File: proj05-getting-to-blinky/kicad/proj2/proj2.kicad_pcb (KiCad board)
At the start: 2 copper layers, 48.3 x 48.3 mm, 7 parts, among them U1 NTE955MC

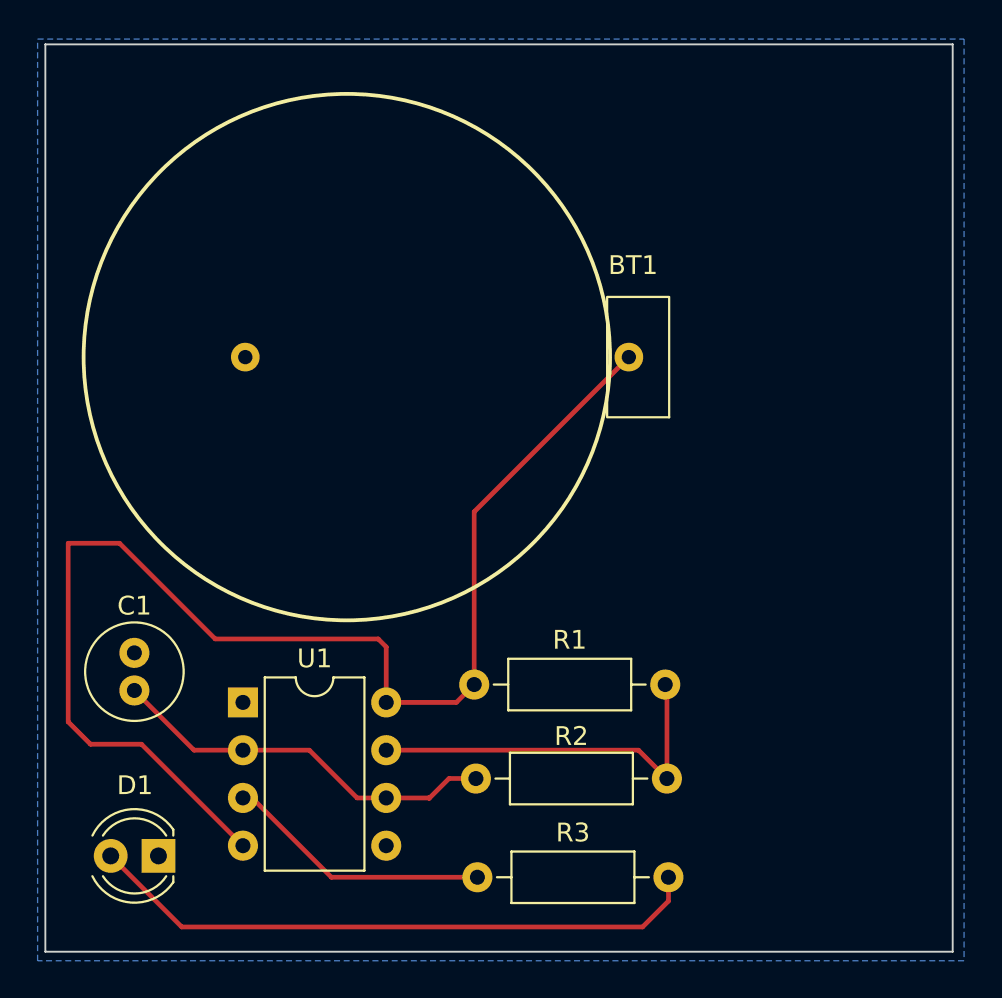
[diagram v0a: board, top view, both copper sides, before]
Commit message: add artwork to proj5
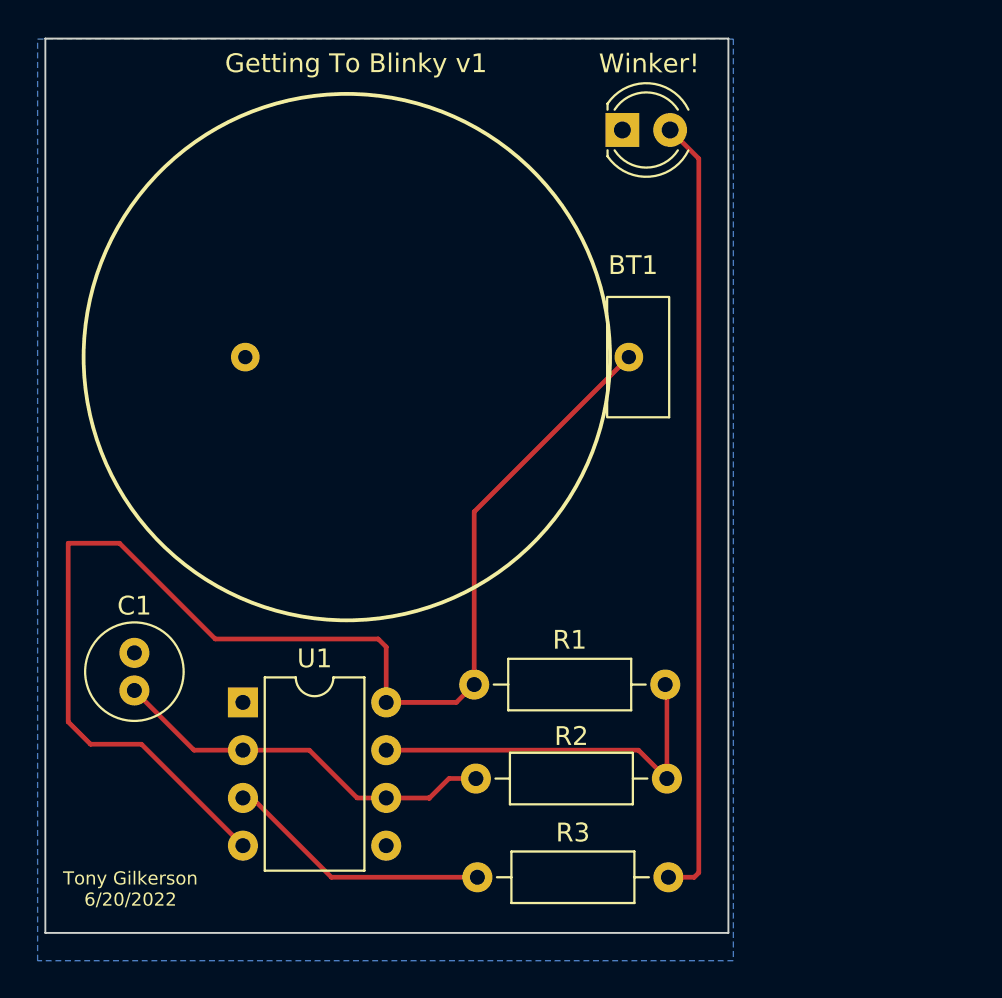
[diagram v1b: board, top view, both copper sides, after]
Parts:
- moved Winker! 45.8 mm to (141.1, 81.3), turned to 0 degrees
- renumbered D1 to Winker!
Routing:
- net Net-(D1-Pad2): track 33.1 -> 41.8 mm
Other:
- board size 48.3 x 48.3 mm -> 36.3 x 47.6 mm
- board text added: "Getting To Blinky v1"
- board text added: "Tony Gilkerson 6/20/2022"
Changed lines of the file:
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@@
   )
   (setup
+    (stackup
+      (layer "F.SilkS" (type "Top Silk Screen"))
+      (layer "F.Paste" (type "Top Solder Paste"))
+      (layer "F.Mask" (type "Top Solder Mask") (thickness 0.01))
+      (layer "F.Cu" (type "copper") (thickness 0.035))
+      (layer "dielectric 1" (type "core") (thickness 1.51) (material "FR4") (epsilon_r 4.5) (loss_tangent 0.02))
+      (layer "B.Cu" (type "copper") (thickness 0.035))
+      (layer "B.Mask" (type "Bottom Solder Mask") (thickness 0.01))
+      (layer "B.Paste" (type "Bottom Solder Paste"))
+      (layer "B.SilkS" (type "Bottom Silk Screen"))
+      (copper_finish "None")
+      (dielectric_constraints no)
+    )
     (pad_to_mask_clearance 0)
     (pcbplotparams
@@
   )
   (footprint "LED_THT:LED_D4.0mm" (layer "F.Cu")
-    (at 116.41 119.9 180)
+    (at 141.085 81.29)
     (descr "LED, diameter 4.0mm, 2 pins, http://www.kingbright.com/attachments/file/psearch/000/00/00/L-43GD(Ver.12B).pdf")
     (tags "LED diameter 4.0mm 2 pins")
@@
     (property "Sheetname" "")
     (attr through_hole)
-    (fp_text reference "D1" (at 1.25 3.75) (layer "F.SilkS")
-      (effects (font (size 1 1) (thickness 0.15)))
-    )
-    (fp_text value "LED" (at 1.27 -3.75) (layer "F.Fab")
+    (fp_text reference "Winker!" (at 1.425 -3.53) (layer "F.SilkS")
+      (effects (font (size 1 1) (thickness 0.15)))
+    )
+    (fp_text value "LED" (at 1.235 3.73) (layer "F.Fab")
       (effects (font (size 1 1) (thickness 0.15)))
     )
@@
     (fp_arc (start -0.73 -1.32665) (mid 3.67 0.000306) (end -0.730339 1.32614) (layer "F.Fab") (width 0.1))
     (fp_circle (center 1.27 0) (end 3.27 0) (layer "F.Fab") (width 0.1) (fill none))
-    (pad "1" thru_hole rect (at 0 0 180) (size 1.8 1.8) (drill 0.9) (layers *.Cu *.Mask)
+    (pad "1" thru_hole rect (at 0 0) (size 1.8 1.8) (drill 0.9) (layers *.Cu *.Mask)
       (net 2 "GND") (pinfunction "K") (pintype "passive"))
-    (pad "2" thru_hole circle (at 2.54 0 180) (size 1.8 1.8) (drill 0.9) (layers *.Cu *.Mask)
+    (pad "2" thru_hole circle (at 2.54 0) (size 1.8 1.8) (drill 0.9) (layers *.Cu *.Mask)
       (net 4 "Net-(D1-Pad2)") (pinfunction "A") (pintype "passive"))
     (model "${KICAD6_3DMODEL_DIR}/LED_THT.3dshapes/LED_D4.0mm.wrl"
@@
       (effects (font (size 1 1) (thickness 0.15)))
     )
-    (fp_text value "NTE955MC" (at 3.81 9.95) (layer "F.Fab")
-      (effects (font (size 1 1) (thickness 0.15)))
-    )
-    (fp_text user "${REFERENCE}" (at 3.81 3.81) (layer "F.Fab")
+    (fp_text value "NTE955MC" (at 3.786 10.244) (layer "F.Fab")
+      (effects (font (size 1 1) (thickness 0.15)))
+    )
+    (fp_text user "${REFERENCE}" (at 3.856 4.434) (layer "F.Fab")
       (effects (font (size 1 1) (thickness 0.15)))
     )
@@
     )
   )
-  (gr_rect (start 110.394 76.736) (end 158.654 124.996) (layer "Edge.Cuts") (width 0.1) (fill none))
+  (gr_line (start 121.15 81.44) (end 120.93 80.81) (layer "B.SilkS") (width 0.15))
+  (gr_line (start 115.91 82.37) (end 115.58 82.81) (layer "B.SilkS") (width 0.15))
+  (gr_circle (center 118.782918 83.97) (end 124.332918 80.87) (layer "B.SilkS") (width 0.15) (fill none))
+  (gr_line (start 121.65 81.44) (end 121.88 80.87) (layer "B.SilkS") (width 0.15))
+  (gr_arc (start 122.022432 85.648649) (mid 118.837206 88.08984) (end 115.542432 85.798649) (layer "B.SilkS") (width 0.2))
+  (gr_line (start 117.14 82.44) (end 117.54 82.89) (layer "B.SilkS") (width 0.15))
+  (gr_line (start 116.84 82.58) (end 117.03 83.08) (layer "B.SilkS") (width 0.15))
+  (gr_line (start 116.56 82.61) (end 116.54 83.2) (layer "B.SilkS") (width 0.15))
+  (gr_line (start 121.89 81.58) (end 122.3 81.17) (layer "B.SilkS") (width 0.15))
+  (gr_line (start 117.45 81.71) (end 115.74 81.71) (layer "B.SilkS") (width 0.15))
+  (gr_line (start 120.88 81.59) (end 120.51 81.17) (layer "B.SilkS") (width 0.15))
+  (gr_line (start 121.38 81.419465) (end 121.38 80.74) (layer "B.SilkS") (width 0.15))
+  (gr_circle (center 121.4 82.26) (end 122.09 81.78) (layer "B.SilkS") (width 0.15) (fill none))
+  (gr_arc (start 117.484999 81.68) (mid 116.582694 82.610496) (end 115.685166 81.675391) (layer "B.SilkS") (width 0.15))
+  (gr_line (start 116.23 82.58) (end 116.02 83.05) (layer "B.SilkS") (width 0.15))
+  (gr_rect (start 110.394 76.426) (end 146.724 123.996) (layer "Edge.Cuts") (width 0.1) (fill none))
+  (gr_text "Tony Gilkerson\n6/20/2022" (at 114.92 121.66) (layer "F.SilkS")
+    (effects (font (size 0.7 0.7) (thickness 0.125)))
+  )
+  (gr_text "Getting To Blinky v1" (at 126.92 77.75) (layer "F.SilkS")
+    (effects (font (size 1 1) (thickness 0.15)))
+  )
   (segment (start 111.61 112.77) (end 111.61 103.27) (width 0.25) (layer "F.Cu") (net 1))
   (segment (start 114.34 103.27) (end 119.43 108.36) (width 0.25) (layer "F.Cu") (net 1))
@@
   (segment (start 128.524 116.816) (end 126.976 116.816) (width 0.25) (layer "F.Cu") (net 3))
   (segment (start 130.786 116.816) (end 128.524 116.816) (width 0.25) (layer "F.Cu") (net 3))
-  (segment (start 117.65 123.68) (end 113.87 119.9) (width 0.25) (layer "F.Cu") (net 4))
-  (segment (start 143.534 122.306) (end 142.16 123.68) (width 0.25) (layer "F.Cu") (net 4))
-  (segment (start 143.534 121.036) (end 143.534 122.306) (width 0.25) (layer "F.Cu") (net 4))
-  (segment (start 142.16 123.68) (end 117.65 123.68) (width 0.25) (layer "F.Cu") (net 4))
+  (segment (start 143.534 121.036) (end 144.904 121.036) (width 0.25) (layer "F.Cu") (net 4))
+  (segment (start 144.904 121.036) (end 145.15 120.79) (width 0.25) (layer "F.Cu") (net 4))
+  (segment (start 145.15 82.815) (end 143.625 81.29) (width 0.25) (layer "F.Cu") (net 4))
+  (segment (start 145.15 120.79) (end 145.15 82.815) (width 0.25) (layer "F.Cu") (net 4))
   (segment (start 128.524 114.276) (end 141.944 114.276) (width 0.25) (layer "F.Cu") (net 5))
   (segment (start 143.454 110.876) (end 143.364 110.786) (width 0.25) (layer "F.Cu") (net 5))
@@
     (polygon
       (pts
-        (xy 159.258 125.476)
+        (xy 146.988 125.476)
         (xy 109.982 125.476)
         (xy 109.982 76.454)
-        (xy 159.258 76.454)
+        (xy 146.988 76.454)
       )
     )

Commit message: add mounting holes proj5
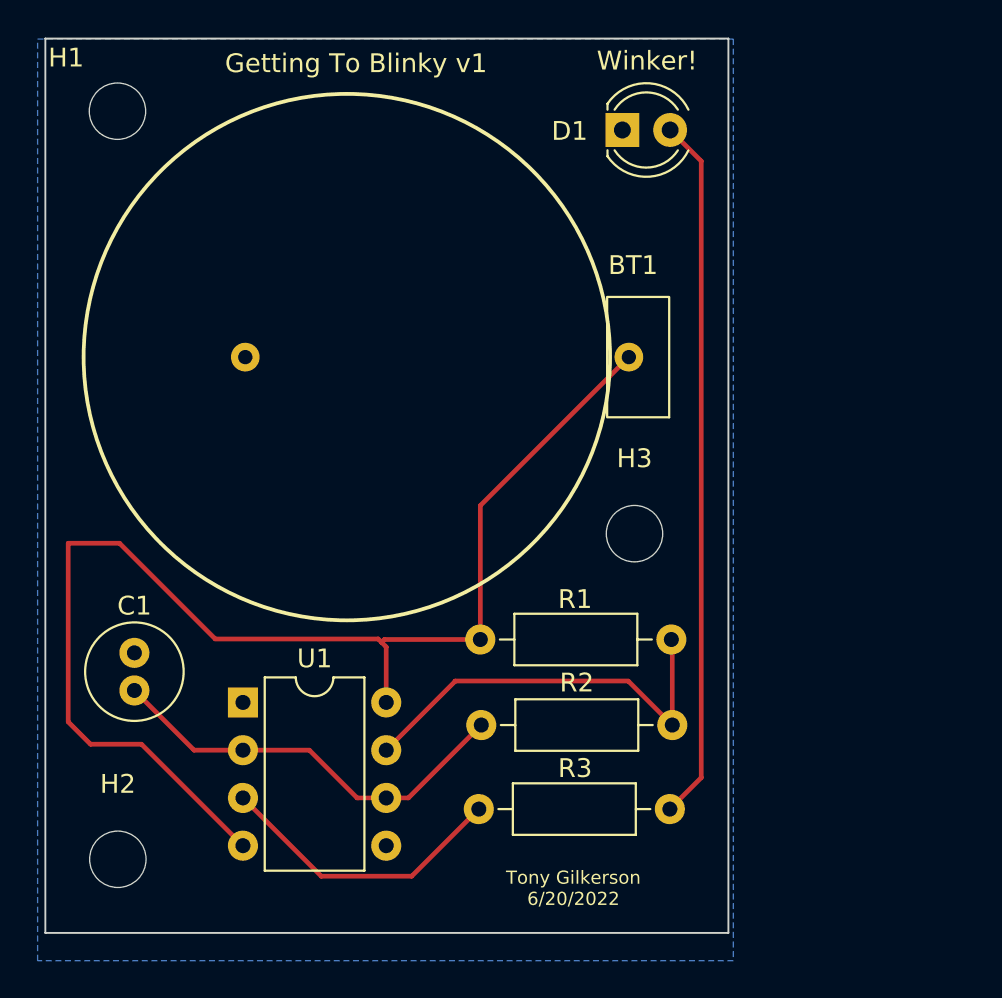
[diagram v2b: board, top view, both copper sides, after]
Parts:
- added H1: MountingHole, MountingHole:MountingHole_3mm, F.Cu at (114.2, 80.3)
- added H2: MountingHole, MountingHole:MountingHole_3mm, F.Cu at (114.2, 120.1)
- added H3: MountingHole, MountingHole:MountingHole_3mm, F.Cu at (141.7, 102.8)
- moved R3 3.63 mm to (133.4, 117.4)
- moved R2 2.86 mm to (143.7, 112.9)
- moved R1 2.42 mm to (133.5, 108.4)
- renumbered Winker! to D1
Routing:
- net Net-(D1-Pad2): track 41.8 -> 37.5 mm
- net Net-(BT1-Pad1): track 69.6 -> 67.3 mm
- net Net-(R1-Pad2): track 20.6 -> 22.3 mm
- net Net-(R3-Pad1): track 14.2 -> 15.7 mm
- net Net-(C1-Pad1): track 21.0 -> 22.4 mm
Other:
- board text added: "Winker!"
